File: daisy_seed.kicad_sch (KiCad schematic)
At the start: 23 parts, among them J3 Micro_SD_Card, J4 SDS-50J, J5 SDS-50J, J6 Conn_02x12_Odd_Even, J7 SDS-50J, U3 Daisy_Seed, U4 H11L1

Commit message: working on output
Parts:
- renumbered D2 to D4
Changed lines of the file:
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@@
 		(dnp no)
 		(fields_autoplaced yes)
-		(property "Reference" "D2"
+		(property "Reference" "D4"
 			(at 184.15 63.4999 90)
 			(effects
@@
 			(project ""
 				(path "/55cca6a8-30da-4c13-b2f2-a01401e2b54c/75aee282-6ddd-4543-b5fc-0fc86bf548ec"
-					(reference "D2")
+					(reference "D4")
 					(unit 1)
 				)

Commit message: fix seed schematic
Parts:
- C10, C9: value C -> 1n C0G
- C11: value C -> 100n
- R10, R11, R7, R8, R9: value R -> 47k
- R12, R17, R18: value R -> 33R
- R13: value R -> 10R
- R14, R15: value R -> 220R
- R16: value R -> 270R
- renumbered J3 to J4, J4 to J5, J5 to J6, J6 to J7, J7 to J8
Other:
- moved on the sheet: C9, R10, R11, R7, R8, R9

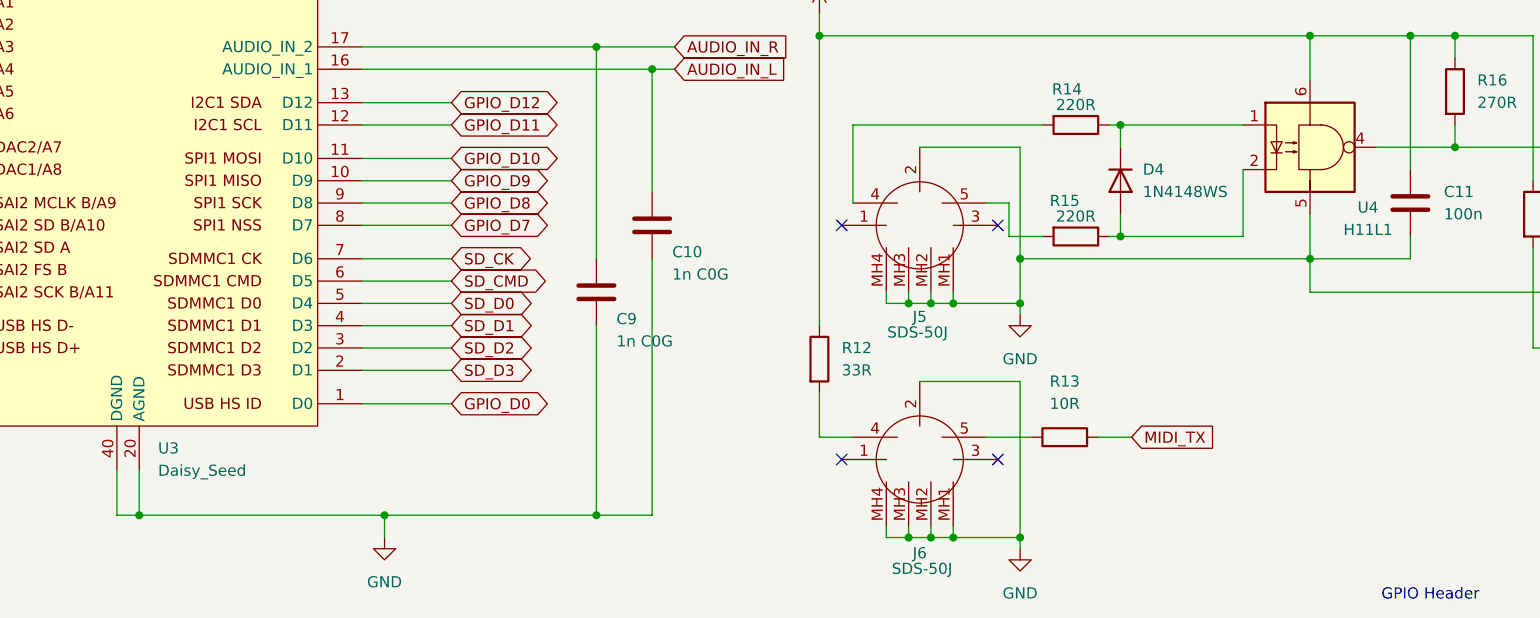
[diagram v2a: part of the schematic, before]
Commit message: change docs to use RS3-1212D
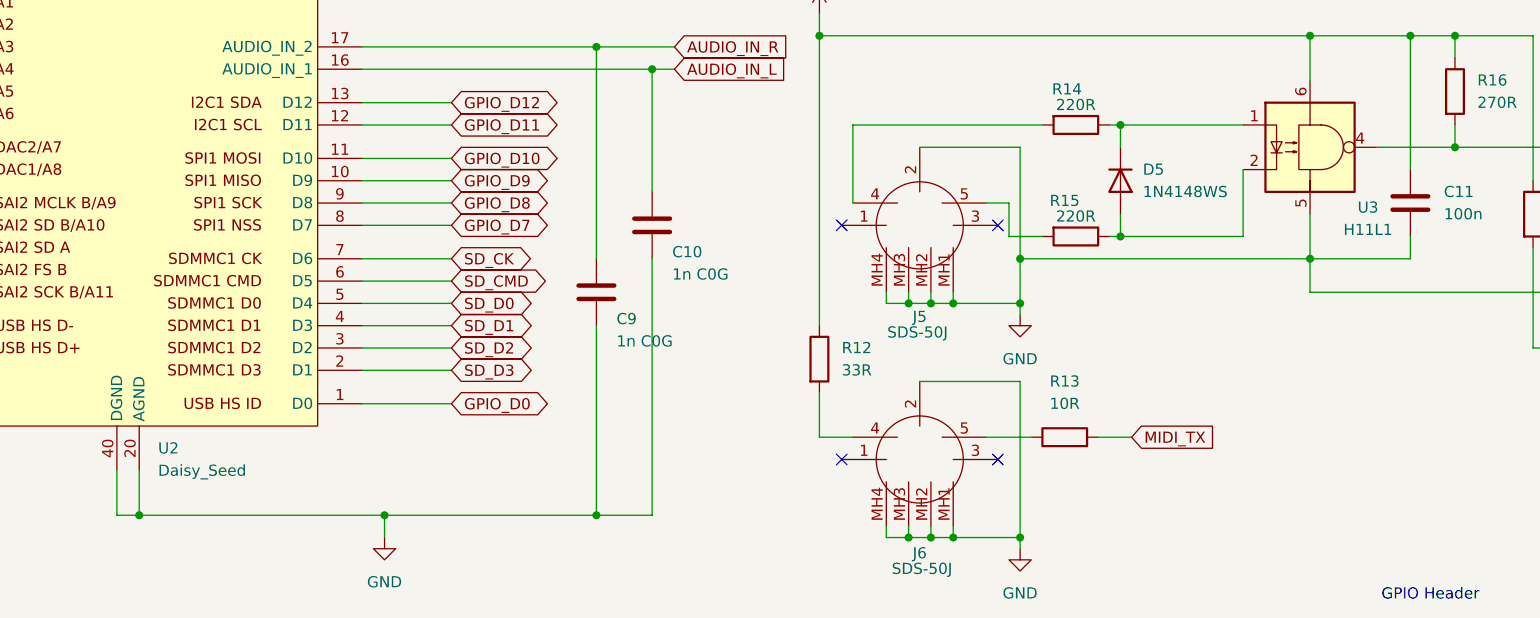
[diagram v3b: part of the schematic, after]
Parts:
- renumbered D4 to D5, U3 to U2, U4 to U3
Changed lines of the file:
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@@
 		(dnp no)
 		(fields_autoplaced yes)
-		(property "Reference" "#PWR028"
+		(property "Reference" "#PWR027"
 			(at 224.79 166.37 0)
 			(effects
@@
 			(project "triptech"
 				(path "/55cca6a8-30da-4c13-b2f2-a01401e2b54c/75aee282-6ddd-4543-b5fc-0fc86bf548ec"
-					(reference "#PWR028")
+					(reference "#PWR027")
 					(unit 1)
 				)
@@
 		(dnp no)
 		(fields_autoplaced yes)
-		(property "Reference" "#PWR026"
+		(property "Reference" "#PWR025"
 			(at 170.18 86.36 0)
 			(effects
@@
 			(project "triptech"
 				(path "/55cca6a8-30da-4c13-b2f2-a01401e2b54c/75aee282-6ddd-4543-b5fc-0fc86bf548ec"
-					(reference "#PWR026")
+					(reference "#PWR025")
 					(unit 1)
 				)
@@
 		(dnp no)
 		(fields_autoplaced yes)
-		(property "Reference" "U3"
+		(property "Reference" "U2"
 			(at 71.9933 95.25 0)
 			(effects
@@
 			(project ""
 				(path "/55cca6a8-30da-4c13-b2f2-a01401e2b54c/75aee282-6ddd-4543-b5fc-0fc86bf548ec"
-					(reference "U3")
+					(reference "U2")
 					(unit 1)
 				)
@@
 		(dnp no)
 		(fields_autoplaced yes)
-		(property "Reference" "#PWR025"
+		(property "Reference" "#PWR024"
 			(at 147.32 49.53 0)
 			(effects
@@
 			(project ""
 				(path "/55cca6a8-30da-4c13-b2f2-a01401e2b54c/75aee282-6ddd-4543-b5fc-0fc86bf548ec"
-					(reference "#PWR025")
+					(reference "#PWR024")
 					(unit 1)
 				)
@@
 		(dnp no)
 		(fields_autoplaced yes)
-		(property "Reference" "#PWR023"
+		(property "Reference" "#PWR022"
 			(at 97.79 111.76 0)
 			(effects
@@
 			(project ""
 				(path "/55cca6a8-30da-4c13-b2f2-a01401e2b54c/75aee282-6ddd-4543-b5fc-0fc86bf548ec"
-					(reference "#PWR023")
+					(reference "#PWR022")
 					(unit 1)
 				)
@@
 		(dnp no)
 		(fields_autoplaced yes)
-		(property "Reference" "#PWR021"
+		(property "Reference" "#PWR020"
 			(at 68.58 27.94 0)
 			(effects
@@
 			(project ""
 				(path "/55cca6a8-30da-4c13-b2f2-a01401e2b54c/75aee282-6ddd-4543-b5fc-0fc86bf548ec"
-					(reference "#PWR021")
+					(reference "#PWR020")
 					(unit 1)
 				)
@@
 		(dnp no)
 		(fields_autoplaced yes)
-		(property "Reference" "#PWR029"
+		(property "Reference" "#PWR028"
 			(at 251.46 111.76 0)
 			(effects
@@
 			(project "triptech"
 				(path "/55cca6a8-30da-4c13-b2f2-a01401e2b54c/75aee282-6ddd-4543-b5fc-0fc86bf548ec"
-					(reference "#PWR029")
+					(reference "#PWR028")
 					(unit 1)
 				)
@@
 		(dnp no)
 		(fields_autoplaced yes)
-		(property "Reference" "#PWR027"
+		(property "Reference" "#PWR026"
 			(at 170.18 113.03 0)
 			(effects
@@
 			(project "triptech"
 				(path "/55cca6a8-30da-4c13-b2f2-a01401e2b54c/75aee282-6ddd-4543-b5fc-0fc86bf548ec"
-					(reference "#PWR027")
+					(reference "#PWR026")
 					(unit 1)
 				)
@@
 		(dnp no)
 		(fields_autoplaced yes)
-		(property "Reference" "#PWR019"
+		(property "Reference" "#PWR018"
 			(at 40.64 123.19 0)
 			(effects
@@
 			(project ""
 				(path "/55cca6a8-30da-4c13-b2f2-a01401e2b54c/75aee282-6ddd-4543-b5fc-0fc86bf548ec"
-					(reference "#PWR019")
+					(reference "#PWR018")
 					(unit 1)
 				)
@@
 		(dnp no)
 		(fields_autoplaced yes)
-		(property "Reference" "#PWR022"
+		(property "Reference" "#PWR021"
 			(at 76.2 27.94 0)
 			(effects
@@
 			(project ""
 				(path "/55cca6a8-30da-4c13-b2f2-a01401e2b54c/75aee282-6ddd-4543-b5fc-0fc86bf548ec"
-					(reference "#PWR022")
+					(reference "#PWR021")
 					(unit 1)
 				)
@@
 		(on_board yes)
 		(dnp no)
-		(property "Reference" "U4"
+		(property "Reference" "U3"
 			(at 209.804 67.818 0)
 			(effects
@@
 			(project ""
 				(path "/55cca6a8-30da-4c13-b2f2-a01401e2b54c/75aee282-6ddd-4543-b5fc-0fc86bf548ec"
-					(reference "U4")
+					(reference "U3")
 					(unit 1)
 				)
@@
 		(dnp no)
 		(fields_autoplaced yes)
-		(property "Reference" "D4"
+		(property "Reference" "D5"
 			(at 184.15 63.4999 90)
 			(effects
@@
 			(project ""
 				(path "/55cca6a8-30da-4c13-b2f2-a01401e2b54c/75aee282-6ddd-4543-b5fc-0fc86bf548ec"
-					(reference "D4")
+					(reference "D5")
 					(unit 1)
 				)
@@
 		(dnp no)
 		(fields_autoplaced yes)
-		(property "Reference" "#PWR020"
+		(property "Reference" "#PWR019"
 			(at 60.96 27.94 0)
 			(effects
@@
 			(project ""
 				(path "/55cca6a8-30da-4c13-b2f2-a01401e2b54c/75aee282-6ddd-4543-b5fc-0fc86bf548ec"
-					(reference "#PWR020")
+					(reference "#PWR019")
 					(unit 1)
 				)
@@
 		(dnp no)
 		(fields_autoplaced yes)
-		(property "Reference" "#PWR024"
+		(property "Reference" "#PWR023"
 			(at 104.14 200.66 0)
 			(effects
@@
 			(project "triptech"
 				(path "/55cca6a8-30da-4c13-b2f2-a01401e2b54c/75aee282-6ddd-4543-b5fc-0fc86bf548ec"
-					(reference "#PWR024")
-					(unit 1)
-				)
+					(reference "#PWR023")
+					(unit 1)
+				)

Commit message: lots of pcb work
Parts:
- removed J4: Micro_SD_Card, Connector_Card:microSD_HC_Hirose_DM3AT-SF-PEJM5, symbol Connector:Micro_SD_Card
- added J4: Micro_SD_Card_Det2, Connector_Card:microSD_HC_Hirose_DM3BT-DSF-PEJS, symbol Connector:Micro_SD_Card_Det2
- J7: footprint Connector_PinHeader_2.54mm:PinHeader_2x12_P2.54mm_Vertical_SMD -> Connector_PinHeader_2.54mm:PinHeader_2x14_P2.54mm_Vertical_SMD; symbol Connector_Generic:Conn_02x12_Odd_Even -> Connector_Generic:Conn_02x14_Odd_Even
- U2: footprint daisy-studio:DAISY_SEED -> daisy-studio:DAISY_SEED_SMT
- U3: footprint Package_SO:SO-6_4.4x3.6mm_P1.27mm -> Package_DIP:SMDIP-6_W7.62mm
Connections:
- net +3V3D: now also J4.4 (VDD)
- net GND: now also J4.11 (SHIELD), J4.6 (VSS); no longer J7.24 (Pin_24)
- net GPIO_D0: no longer J7.1 (Pin_1)
- net GPIO_D10: now also J7.7 (Pin_7); no longer J7.9 (Pin_9)
- net GPIO_D11: now also J7.5 (Pin_5); no longer J7.11 (Pin_11)
- net GPIO_D12: now also J7.3 (Pin_3); no longer J7.13 (Pin_13)
- net GPIO_D15: no longer J7.2 (Pin_2)
- net GPIO_D16: no longer J7.4 (Pin_4)
- net GPIO_D17: no longer J7.6 (Pin_6)
- net GPIO_D18: no longer J7.8 (Pin_8)
- net GPIO_D19: no longer J7.10 (Pin_10)
- net GPIO_D20: no longer J7.12 (Pin_12)
- net GPIO_D21: no longer J7.14 (Pin_14)
- net GPIO_D22: no longer J7.16 (Pin_16)
- net GPIO_D23: no longer J7.18 (Pin_18)
- net GPIO_D24: no longer J7.20 (Pin_20)
- net GPIO_D25: no longer J7.22 (Pin_22)
- net GPIO_D26: no longer J7.23 (Pin_23)
- net GPIO_D27: no longer J7.21 (Pin_21)
- net GPIO_D28: no longer J7.19 (Pin_19)
- net GPIO_D29: no longer J7.15 (Pin_15)
- net GPIO_D30: no longer J7.17 (Pin_17)
- net GPIO_D7: now also J7.13 (Pin_13); no longer J7.3 (Pin_3)
- net GPIO_D8: now also J7.11 (Pin_11); no longer J7.5 (Pin_5)
- net GPIO_D9: now also J7.9 (Pin_9); no longer J7.7 (Pin_7)
- net SD_CK: now also J4.5 (CLK)
- net SD_CMD: now also J4.3 (CMD)
- net SD_D0: now also J4.7 (DAT0)
- net SD_D1: now also J4.8 (DAT1)
- net SD_D2: now also J4.1 (DAT2)
- net SD_D3: now also J4.2 (DAT3/CD)
- no-connect marks 6 -> 8

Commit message: lots of pcb work
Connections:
- net GND: now also J7.26 (Pin_26), J7.27 (Pin_27), J7.28 (Pin_28)
- net GPIO_D0: now also J7.4 (Pin_4)
- net GPIO_D15: now also J7.15 (Pin_15)
- net GPIO_D16: now also J7.17 (Pin_17)
- net GPIO_D17: now also J7.19 (Pin_19)
- net GPIO_D18: now also J7.21 (Pin_21)
- net GPIO_D19: now also J7.23 (Pin_23)
- net GPIO_D20: now also J7.25 (Pin_25)
- net GPIO_D21: now also J7.6 (Pin_6)
- net GPIO_D22: now also J7.8 (Pin_8)
- net GPIO_D23: now also J7.10 (Pin_10)
- net GPIO_D24: now also J7.12 (Pin_12)
- net GPIO_D25: now also J7.14 (Pin_14)
- net GPIO_D26: now also J7.16 (Pin_16)
- net GPIO_D27: now also J7.18 (Pin_18)
- net GPIO_D28: now also J7.20 (Pin_20)
- net GPIO_D29: now also J7.22 (Pin_22)
- net GPIO_D30: now also J7.24 (Pin_24)

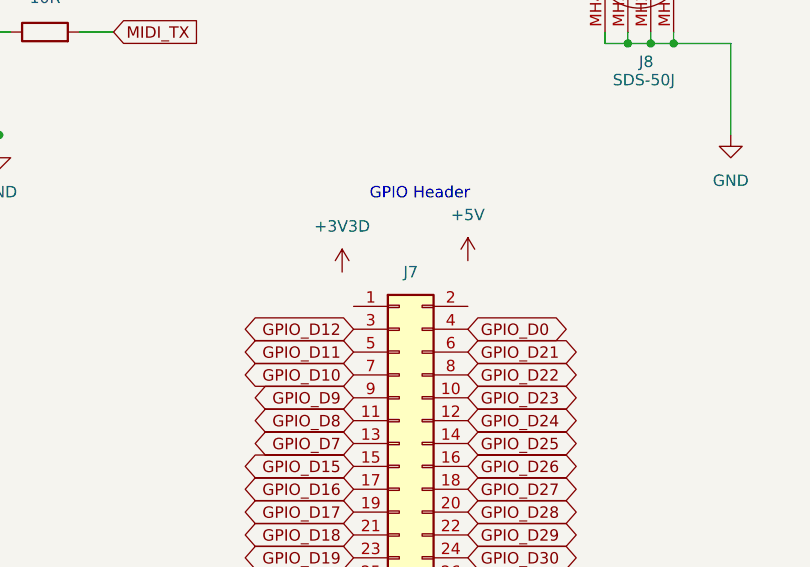
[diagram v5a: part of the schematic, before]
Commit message: clean up some power cap issues
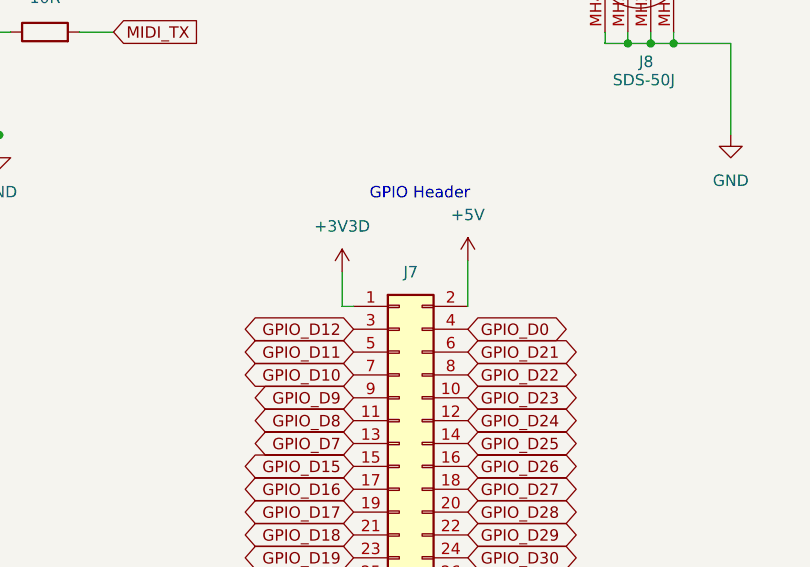
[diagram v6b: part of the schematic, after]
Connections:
- net +3V3D: now also J7.1 (Pin_1)
- net +5V: now also J7.2 (Pin_2)
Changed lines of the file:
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@@
 	(wire
 		(pts
+			(xy 208.28 124.46) (xy 209.55 124.46)
+		)
+		(stroke
+			(width 0)
+			(type default)
+		)
+	)
+	(wire
+		(pts
 			(xy 162.56 78.74) (xy 170.18 78.74)
 		)
@@
 	(wire
 		(pts
+			(xy 222.25 119.38) (xy 222.25 124.46)
+		)
+		(stroke
+			(width 0)
+			(type default)
+		)
+	)
+	(wire
+		(pts
 			(xy 52.07 121.92) (xy 52.07 132.08)
 		)
@@
 	(wire
 		(pts
+			(xy 208.28 120.65) (xy 208.28 124.46)
+		)
+		(stroke
+			(width 0)
+			(type default)
+		)
+	)
+	(wire
+		(pts
 			(xy 34.29 180.34) (xy 52.07 180.34)
 		)
@@
 		(dnp no)
 		(fields_autoplaced yes)
-		(property "Reference" "#PWR030"
+		(property "Reference" "#PWR029"
 			(at 215.9 166.37 0)
 			(effects
@@
 			(project "triptech"
 				(path "/55cca6a8-30da-4c13-b2f2-a01401e2b54c/75aee282-6ddd-4543-b5fc-0fc86bf548ec"
-					(reference "#PWR030")
+					(reference "#PWR029")
 					(unit 1)
 				)
@@
 		(dnp no)
 		(fields_autoplaced yes)
-		(property "Reference" "#PWR029"
+		(property "Reference" "#PWR030"
 			(at 222.25 123.19 0)
 			(effects
@@
 			(project "daisy-studio"
 				(path "/55cca6a8-30da-4c13-b2f2-a01401e2b54c/75aee282-6ddd-4543-b5fc-0fc86bf548ec"
-					(reference "#PWR029")
+					(reference "#PWR030")
 					(unit 1)
 				)

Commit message: final layout
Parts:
- renumbered C10 to C33, C9 to C34, C11 to C35, D5 to D11, J5 to J10, J7 to J11, J4 to J14, J8 to J7, J6 to J9, R12 to R21, R17 to R22, R18 to R23, R14 to R24, R9 to R25, R11 to R26, R7 to R27, R10 to R28, R13 to R29, R16 to R30, R15 to R31, R8 to R32, U3 to U8, U2 to U9
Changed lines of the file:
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@@
 		(dnp no)
 		(fields_autoplaced yes)
-		(property "Reference" "U2"
+		(property "Reference" "U9"
 			(at 71.9933 95.25 0)
 			(effects
@@
 			(project ""
 				(path "/55cca6a8-30da-4c13-b2f2-a01401e2b54c/75aee282-6ddd-4543-b5fc-0fc86bf548ec"
-					(reference "U2")
+					(reference "U9")
 					(unit 1)
 				)
@@
 		(dnp no)
 		(fields_autoplaced yes)
-		(property "Reference" "C11"
+		(property "Reference" "C35"
 			(at 218.44 66.0399 0)
 			(effects
@@
 			(project ""
 				(path "/55cca6a8-30da-4c13-b2f2-a01401e2b54c/75aee282-6ddd-4543-b5fc-0fc86bf548ec"
-					(reference "C11")
+					(reference "C35")
 					(unit 1)
 				)
@@
 		(on_board yes)
 		(dnp no)
-		(property "Reference" "C10"
+		(property "Reference" "C33"
 			(at 130.556 72.898 0)
 			(effects
@@
 			(project ""
 				(path "/55cca6a8-30da-4c13-b2f2-a01401e2b54c/75aee282-6ddd-4543-b5fc-0fc86bf548ec"
-					(reference "C10")
+					(reference "C33")
 					(unit 1)
 				)
@@
 		(on_board yes)
 		(dnp no)
-		(property "Reference" "R14"
+		(property "Reference" "R24"
 			(at 175.514 54.356 90)
 			(effects
@@
 			(project ""
 				(path "/55cca6a8-30da-4c13-b2f2-a01401e2b54c/75aee282-6ddd-4543-b5fc-0fc86bf548ec"
-					(reference "R14")
+					(reference "R24")
 					(unit 1)
 				)
@@
 		(on_board yes)
 		(dnp no)
-		(property "Reference" "R9"
+		(property "Reference" "R25"
 			(at 45.72 146.05 90)
 			(effects
@@
 			(project "triptech"
 				(path "/55cca6a8-30da-4c13-b2f2-a01401e2b54c/75aee282-6ddd-4543-b5fc-0fc86bf548ec"
-					(reference "R9")
+					(reference "R25")
 					(unit 1)
 				)
@@
 		(on_board yes)
 		(dnp no)
-		(property "Reference" "C9"
+		(property "Reference" "C34"
 			(at 124.206 80.518 0)
 			(effects
@@
 			(project "daisy-studio"
 				(path "/55cca6a8-30da-4c13-b2f2-a01401e2b54c/75aee282-6ddd-4543-b5fc-0fc86bf548ec"
-					(reference "C9")
+					(reference "C34")
 					(unit 1)
 				)
@@
 		(on_board yes)
 		(dnp no)
-		(property "Reference" "J5"
+		(property "Reference" "J10"
 			(at 158.75 80.264 0)
 			(effects
@@
 			(project ""
 				(path "/55cca6a8-30da-4c13-b2f2-a01401e2b54c/75aee282-6ddd-4543-b5fc-0fc86bf548ec"
-					(reference "J5")
+					(reference "J10")
 					(unit 1)
 				)
@@
 		(on_board yes)
 		(dnp no)
-		(property "Reference" "R18"
+		(property "Reference" "R23"
 			(at 254 68.5799 0)
 			(effects
@@
 			(project "triptech"
 				(path "/55cca6a8-30da-4c13-b2f2-a01401e2b54c/75aee282-6ddd-4543-b5fc-0fc86bf548ec"
-					(reference "R18")
+					(reference "R23")
 					(unit 1)
 				)
@@
 		(on_board yes)
 		(dnp no)
-		(property "Reference" "R8"
+		(property "Reference" "R32"
 			(at 41.91 153.67 90)
 			(effects
@@
 			(project "triptech"
 				(path "/55cca6a8-30da-4c13-b2f2-a01401e2b54c/75aee282-6ddd-4543-b5fc-0fc86bf548ec"
-					(reference "R8")
+					(reference "R32")
 					(unit 1)
 				)
@@
 		(on_board yes)
 		(dnp no)
-		(property "Reference" "J7"
+		(property "Reference" "J11"
 			(at 215.9 120.65 0)
 			(effects
@@
 			(project ""
 				(path "/55cca6a8-30da-4c13-b2f2-a01401e2b54c/75aee282-6ddd-4543-b5fc-0fc86bf548ec"
-					(reference "J7")
+					(reference "J11")
 					(unit 1)
 				)
@@
 		(dnp no)
 		(fields_autoplaced yes)
-		(property "Reference" "R17"
+		(property "Reference" "R22"
 			(at 231.14 67.3099 0)
 			(effects
@@
 			(project ""
 				(path "/55cca6a8-30da-4c13-b2f2-a01401e2b54c/75aee282-6ddd-4543-b5fc-0fc86bf548ec"
-					(reference "R17")
+					(reference "R22")
 					(unit 1)
 				)
@@
 		(dnp no)
 		(fields_autoplaced yes)
-		(property "Reference" "R12"
+		(property "Reference" "R21"
 			(at 149.86 83.8199 0)
 			(effects
@@
 			(project "triptech"
 				(path "/55cca6a8-30da-4c13-b2f2-a01401e2b54c/75aee282-6ddd-4543-b5fc-0fc86bf548ec"
-					(reference "R12")
+					(reference "R21")
 					(unit 1)
 				)
@@
 		(on_board yes)
 		(dnp no)
-		(property "Reference" "R11"
+		(property "Reference" "R26"
 			(at 53.34 130.81 90)
 			(effects
@@
 			(project "triptech"
 				(path "/55cca6a8-30da-4c13-b2f2-a01401e2b54c/75aee282-6ddd-4543-b5fc-0fc86bf548ec"
-					(reference "R11")
+					(reference "R26")
 					(unit 1)
 				)
@@
 		(on_board yes)
 		(dnp no)
-		(property "Reference" "U3"
+		(property "Reference" "U8"
 			(at 209.804 67.818 0)
 			(effects
@@
 			(project ""
 				(path "/55cca6a8-30da-4c13-b2f2-a01401e2b54c/75aee282-6ddd-4543-b5fc-0fc86bf548ec"
-					(reference "U3")
+					(reference "U8")
 					(unit 1)
 				)
@@
 		(on_board yes)
 		(dnp no)
-		(property "Reference" "J6"
+		(property "Reference" "J9"
 			(at 158.75 107.188 0)
 			(effects
@@
 			(project "triptech"
 				(path "/55cca6a8-30da-4c13-b2f2-a01401e2b54c/75aee282-6ddd-4543-b5fc-0fc86bf548ec"
-					(reference "J6")
+					(reference "J9")
 					(unit 1)
 				)
@@
 		(on_board yes)
 		(dnp no)
-		(property "Reference" "R10"
+		(property "Reference" "R28"
 			(at 49.53 138.43 90)
 			(effects
@@
 			(project "triptech"
 				(path "/55cca6a8-30da-4c13-b2f2-a01401e2b54c/75aee282-6ddd-4543-b5fc-0fc86bf548ec"
-					(reference "R10")
+					(reference "R28")
 					(unit 1)
 				)
@@
 		(on_board yes)
 		(dnp no)
-		(property "Reference" "J8"
+		(property "Reference" "J7"
 			(at 242.062 97.282 0)
 			(effects
@@
 			(project "triptech"
 				(path "/55cca6a8-30da-4c13-b2f2-a01401e2b54c/75aee282-6ddd-4543-b5fc-0fc86bf548ec"
-					(reference "J8")
+					(reference "J7")
 					(unit 1)
 				)
@@
 		(dnp no)
 		(fields_autoplaced yes)
-		(property "Reference" "D5"
+		(property "Reference" "D11"
 			(at 184.15 63.4999 90)
 			(effects
@@
 			(project ""
 				(path "/55cca6a8-30da-4c13-b2f2-a01401e2b54c/75aee282-6ddd-4543-b5fc-0fc86bf548ec"
-					(reference "D5")
+					(reference "D11")
 					(unit 1)
 				)
@@
 		(on_board yes)
 		(dnp no)
-		(property "Reference" "R15"
+		(property "Reference" "R31"
 			(at 175.26 67.056 90)
 			(effects
@@
 			(project "triptech"
 				(path "/55cca6a8-30da-4c13-b2f2-a01401e2b54c/75aee282-6ddd-4543-b5fc-0fc86bf548ec"
-					(reference "R15")
+					(reference "R31")
 					(unit 1)
 				)
@@
 		(dnp no)
 		(fields_autoplaced yes)
-		(property "Reference" "J4"
+		(property "Reference" "J14"
 			(at 84.455 153.67 0)
 			(effects
@@
 			(project ""
 				(path "/55cca6a8-30da-4c13-b2f2-a01401e2b54c/75aee282-6ddd-4543-b5fc-0fc86bf548ec"
-					(reference "J4")
+					(reference "J14")
 					(unit 1)
 				)
@@
 		(dnp no)
 		(fields_autoplaced yes)
-		(property "Reference" "R16"
+		(property "Reference" "R30"
 			(at 222.25 53.3399 0)
 			(effects
@@
 			(project ""
 				(path "/55cca6a8-30da-4c13-b2f2-a01401e2b54c/75aee282-6ddd-4543-b5fc-0fc86bf548ec"
-					(reference "R16")
+					(reference "R30")
 					(unit 1)
 				)
@@
 		(on_board yes)
 		(dnp no)
-		(property "Reference" "R7"
+		(property "Reference" "R27"
 			(at 38.1 161.29 90)
 			(effects
@@
 			(project ""
 				(path "/55cca6a8-30da-4c13-b2f2-a01401e2b54c/75aee282-6ddd-4543-b5fc-0fc86bf548ec"
-					(reference "R7")
+					(reference "R27")
 					(unit 1)
 				)
@@
 		(dnp no)
 		(fields_autoplaced yes)
-		(property "Reference" "R13"
+		(property "Reference" "R29"
 			(at 175.26 87.63 90)
 			(effects
@@
 			(project "triptech"
 				(path "/55cca6a8-30da-4c13-b2f2-a01401e2b54c/75aee282-6ddd-4543-b5fc-0fc86bf548ec"
-					(reference "R13")
-					(unit 1)
-				)
+					(reference "R29")
+					(unit 1)
+				)
